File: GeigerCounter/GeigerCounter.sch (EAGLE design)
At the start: 5 parts, among them IC1 OPAMP-DUALU

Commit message: preliminary schematic work
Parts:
- added C2, C3, C4, C5, C6: (no value), SparkFun-Passives:CAPPTH2
- added H1, H2, H3, H4: MOUNT-HOLE3.0, holes:MOUNT-HOLE3.0
- added IC2: OPAMP-DUALU, SparkFun-AnalogIC:OPAMP-DUALU
- added R10, R11, R12, R13, R14, R15, R16, R18, R19, R2, R20, R22, R3, R4, R5, R6, R7, R8, R9: (no value), SparkFun-Passives:RESISTORAXIAL-0.3
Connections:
- new net N$1: C3.2, R3.1
- new net N$10: C4.2, IC2A.OUT, R12.2, R14.2, R15.1
- new net N$11: C4.1, IC2A.-IN, R12.1, R14.1
- new net N$12: C5.1, R15.2
- new net N$13: C5.2, R13.1
- new net N$14: C6.1, IC2B.-IN, R18.1, R19.1, R8.2
- new net N$15: C6.2, IC2B.OUT, R18.2, R19.2, R20.1
- new net N$2: D1.A, R9.1
- new net N$3: C2.2, IC1A.OUT, R10.2, R11.1, R2.2
- new net N$4: IC2B.+IN, R13.2, R16.2
- new net N$5: D1.C, R22.1
- new net N$6: C2.1, IC1A.-IN, R10.1, R2.1
- new net N$7: C3.1, R11.2
- new net N$8: C1.1, IC1B.-IN, R3.2, R5.1, R6.1
- new net N$9: C1.2, IC1B.OUT, R5.2, R6.2, R7.1
- new net VCC_1.25: IC1A.+IN, IC1B.+IN, R1.2, R4.1
- net GND: now also IC1A.V-, IC2A.+IN, IC2A.V-, R1.1, R16.1, R8.1
- net VCC: now also IC1A.V+, IC2A.V+, R4.2
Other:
- moved on the sheet: C1, D1, IC1A, IC1B, R1, U$1

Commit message: all components placed in schematic
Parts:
- added C10, C8: 0.1uF, SparkFun-Passives:CAPPTH2
- added C7, C9: 2.2uF, SparkFun-Passives:CAPPTH2
- added R17, R21, R23, R24: DNP, SparkFun-Passives:RESISTORAXIAL-0.3
- added R25, R26: 0, SparkFun-Passives:RESISTORAXIAL-0.3
- C1, C6, R12, R18, R2, R22, R5, R9: value (none) -> DNP
- C2, C4: value (none) -> 2pF
- C3, C5: value (none) -> 100pF
- R1, R4: value (none) -> 1k
- R10, R14: value (none) -> 10 MEGA
- R11, R13, R15, R20, R7: value (none) -> 0
- R16, R3, R8: value (none) -> 10k
- R19, R6: value (none) -> 100k
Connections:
- new net N$16: R26.1, R7.2
- new net N$17: C1.1, R24.1, R25.2
- new net N$20: C6.1, R23.1, R26.2
- new net N$21: R20.2, R25.1
- net GND: now also C1.2, C10.1, C6.2, C7.1, C8.1, C9.1, R9.2
- net N$11: now also R21.2
- net N$14: no longer C6.1
- net N$15: no longer C6.2
- net N$2: now also R17.1
- net N$5: now also R21.1
- net N$6: now also R17.2
- net N$8: no longer C1.1
- net N$9: no longer C1.2
- net P3.4: now also R24.2
- net P3.5: now also R23.2
- net VCC: now also C10.2, C7.2, C8.2, C9.2
- net VCC_1.25: now also R22.2
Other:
- moved on the sheet: C1, C6, D1, H1, H2, H3, H4, R10, R12, R14, R18, R2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

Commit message: Added header pins as well as cleaned up schematic a bit. Also added test points
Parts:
- removed R17, R21, R22, R9: DNP, SparkFun-Passives:RESISTORAXIAL-0.3
- removed R20, R26: 0, SparkFun-Passives:RESISTORAXIAL-0.3
- added TP_GND, TP_INV1, TP_INV2, TP_POS1, TP_POS2, TP_VCC: PTR1PAD1-20, testpad:PTR1PAD1-20
- added U$2: M04X2, SparkFun-Connectors:M04X2
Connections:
- removed net N$20: C6.1, R23.1, R26.2
- removed net N$21: R20.2, R25.1
- net GND: now also TP_GND.TP, U$2.4; no longer R9.2
- net N$11: now also U$2.8; no longer R21.2
- net N$12: now also TP_POS1.TP
- net N$15: now also R25.1, TP_POS2.TP; no longer R20.1
- net N$16: now also C6.1, R23.1; no longer R26.1
- net N$2: now also D1.C, U$2.5, U$2.7; no longer D1.A, R17.1, R9.1
- net N$5: now also D1.A, U$2.1, U$2.3; no longer D1.C, R21.1, R22.1
- net N$6: now also U$2.2; no longer R17.2
- net N$7: now also TP_INV1.TP
- net N$9: now also TP_INV2.TP
- net VCC: now also TP_VCC.TP
- net VCC_1.25: now also U$2.6; no longer R22.2
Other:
- note added: "Access ID: 4841"
- note added: "Decoupling Caps for IC1"
- note added: "Decoupling Caps for IC2"
- note added: "Web ID: 49211282"
- moved on the sheet: D1, R25, R7

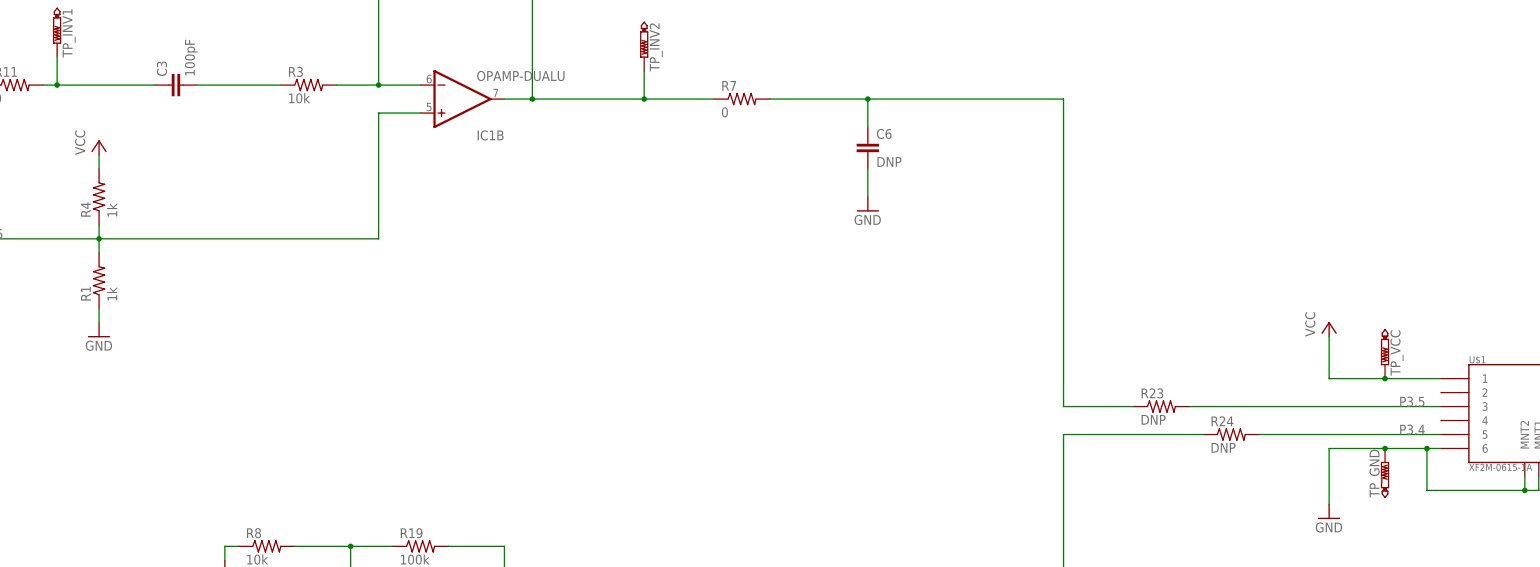
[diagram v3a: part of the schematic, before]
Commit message: Updated with new connector on output
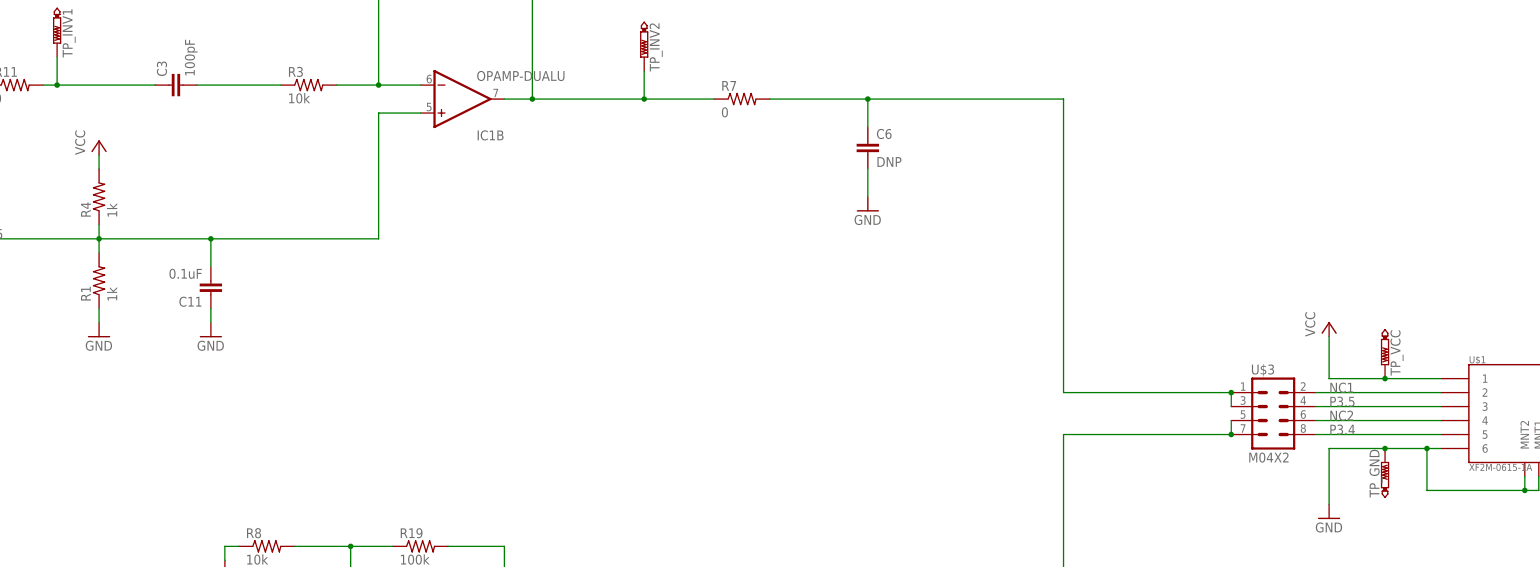
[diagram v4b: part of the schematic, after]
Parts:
- removed R23, R24: DNP, SparkFun-Passives:RESISTORAXIAL-0.3
- added C11: 0.1uF, SparkFun-Passives:CAPPTH2
- added U$3: M04X2, SparkFun-Connectors:M04X2
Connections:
- new net NC1: U$1.2, U$3.2
- new net NC2: U$1.4, U$3.6
- net GND: now also C11.1
- net N$16: now also U$3.1, U$3.3; no longer R23.1
- net N$17: now also U$3.5, U$3.7; no longer R24.1
- net P3.4: now also U$3.8; no longer R24.2
- net P3.5: now also U$3.4; no longer R23.2
- net VCC_1.25: now also C11.2
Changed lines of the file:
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@@
 <part name="P+8" library="supply1" deviceset="VCC" device=""/>
 <part name="GND12" library="supply1" deviceset="GND" device=""/>
-<part name="R23" library="SparkFun-Passives" deviceset="RESISTOR" device="AXIAL-0.3" value="DNP"/>
-<part name="R24" library="SparkFun-Passives" deviceset="RESISTOR" device="AXIAL-0.3" value="DNP"/>
 <part name="R25" library="SparkFun-Passives" deviceset="RESISTOR" device="AXIAL-0.3" value="0"/>
 <part name="C1" library="SparkFun-Passives" deviceset="CAP" device="PTH2" value="DNP"/>
@@
 <part name="TP_POS2" library="testpad" deviceset="PTR1" device="PAD1-20"/>
 <part name="U$2" library="SparkFun-Connectors" deviceset="M04X2" device=""/>
+<part name="C11" library="SparkFun-Passives" deviceset="CAP" device="PTH2" value="0.1uF"/>
+<part name="GND15" library="supply1" deviceset="GND" device=""/>
+<part name="U$3" library="SparkFun-Connectors" deviceset="M04X2" device=""/>
 </parts>
 <sheets>
@@
 <instance part="P+8" gate="VCC" x="73.66" y="71.12"/>
 <instance part="GND12" gate="1" x="35.56" y="96.52"/>
-<instance part="R23" gate="G$1" x="360.68" y="99.06"/>
-<instance part="R24" gate="G$1" x="373.38" y="93.98"/>
 <instance part="R25" gate="G$1" x="284.48" y="38.1"/>
 <instance part="C1" gate="G$1" x="304.8" y="27.94"/>
@@
 <instance part="TP_POS2" gate="G$1" x="264.16" y="45.72" rot="R180"/>
 <instance part="U$2" gate="G$1" x="25.4" y="104.14"/>
+<instance part="C11" gate="G$1" x="187.96" y="121.92" rot="R180"/>
+<instance part="GND15" gate="1" x="187.96" y="111.76"/>
+<instance part="U$3" gate="G$1" x="381" y="96.52"/>
 </instances>
 <busses>
@@
 <pinref part="GND12" gate="1" pin="GND"/>
 </segment>
+<segment>
+<pinref part="C11" gate="G$1" pin="1"/>
+<wire x1="187.96" y1="116.84" x2="187.96" y2="114.3" width="0.1524" layer="91"/>
+<pinref part="GND15" gate="1" pin="GND"/>
+</segment>
 </net>
 <net name="P3.5" class="0">
 <segment>
-<label x="403.86" y="99.06" size="1.778" layer="95"/>
+<label x="391.16" y="99.06" size="1.778" layer="95"/>
 <pinref part="U$1" gate="P$1" pin="3"/>
-<pinref part="R23" gate="G$1" pin="2"/>
-<wire x1="365.76" y1="99.06" x2="411.48" y2="99.06" width="0.1524" layer="91"/>
+<wire x1="388.62" y1="99.06" x2="411.48" y2="99.06" width="0.1524" layer="91"/>
+<pinref part="U$3" gate="G$1" pin="4"/>
 </segment>
 </net>
 <net name="P3.4" class="0">
 <segment>
-<label x="403.86" y="93.98" size="1.778" layer="95"/>
+<label x="391.16" y="93.98" size="1.778" layer="95"/>
 <pinref part="U$1" gate="P$1" pin="5"/>
-<pinref part="R24" gate="G$1" pin="2"/>
-<wire x1="378.46" y1="93.98" x2="411.48" y2="93.98" width="0.1524" layer="91"/>
+<wire x1="388.62" y1="93.98" x2="411.48" y2="93.98" width="0.1524" layer="91"/>
+<pinref part="U$3" gate="G$1" pin="8"/>
 </segment>
 </net>
@@
 <wire x1="226.06" y1="152.4" x2="218.44" y2="152.4" width="0.1524" layer="91"/>
 <wire x1="218.44" y1="152.4" x2="218.44" y2="129.54" width="0.1524" layer="91"/>
-<wire x1="218.44" y1="129.54" x2="167.64" y2="129.54" width="0.1524" layer="91"/>
+<wire x1="218.44" y1="129.54" x2="187.96" y2="129.54" width="0.1524" layer="91"/>
 <junction x="167.64" y="129.54"/>
+<wire x1="187.96" y1="129.54" x2="167.64" y2="129.54" width="0.1524" layer="91"/>
 <wire x1="167.64" y1="129.54" x2="104.14" y2="129.54" width="0.1524" layer="91"/>
 <wire x1="104.14" y1="129.54" x2="104.14" y2="154.94" width="0.1524" layer="91"/>
@@
 <wire x1="33.02" y1="104.14" x2="48.26" y2="104.14" width="0.1524" layer="91"/>
 <wire x1="48.26" y1="104.14" x2="48.26" y2="154.94" width="0.1524" layer="91"/>
+<pinref part="C11" gate="G$1" pin="2"/>
+<wire x1="187.96" y1="124.46" x2="187.96" y2="129.54" width="0.1524" layer="91"/>
+<junction x="187.96" y="129.54"/>
 </segment>
 </net>
@@
 <wire x1="304.8" y1="38.1" x2="304.8" y2="33.02" width="0.1524" layer="91"/>
 <wire x1="342.9" y1="38.1" x2="342.9" y2="93.98" width="0.1524" layer="91"/>
-<pinref part="R24" gate="G$1" pin="1"/>
-<wire x1="342.9" y1="93.98" x2="368.3" y2="93.98" width="0.1524" layer="91"/>
 <wire x1="304.8" y1="38.1" x2="342.9" y2="38.1" width="0.1524" layer="91"/>
 <junction x="304.8" y="38.1"/>
+<pinref part="U$3" gate="G$1" pin="7"/>
+<wire x1="373.38" y1="93.98" x2="342.9" y2="93.98" width="0.1524" layer="91"/>
+<pinref part="U$3" gate="G$1" pin="5"/>
+<wire x1="373.38" y1="96.52" x2="373.38" y2="93.98" width="0.1524" layer="91"/>
+<junction x="373.38" y="93.98"/>
 </segment>
 </net>
@@
 <wire x1="307.34" y1="154.94" x2="307.34" y2="149.86" width="0.1524" layer="91"/>
 <wire x1="307.34" y1="154.94" x2="342.9" y2="154.94" width="0.1524" layer="91"/>
-<wire x1="342.9" y1="154.94" x2="342.9" y2="99.06" width="0.1524" layer="91"/>
+<wire x1="342.9" y1="154.94" x2="342.9" y2="101.6" width="0.1524" layer="91"/>
 <junction x="307.34" y="154.94"/>
-<pinref part="R23" gate="G$1" pin="1"/>
-<wire x1="342.9" y1="99.06" x2="355.6" y2="99.06" width="0.1524" layer="91"/>
+<pinref part="U$3" gate="G$1" pin="1"/>
+<wire x1="373.38" y1="101.6" x2="342.9" y2="101.6" width="0.1524" layer="91"/>
+<pinref part="U$3" gate="G$1" pin="3"/>
+<wire x1="373.38" y1="99.06" x2="373.38" y2="101.6" width="0.1524" layer="91"/>
+<junction x="373.38" y="101.6"/>
 </segment>
 </net>
@@
 </segment>
 </net>
+<net name="NC1" class="0">
+<segment>
+<pinref part="U$1" gate="P$1" pin="2"/>
+<wire x1="411.48" y1="101.6" x2="388.62" y2="101.6" width="0.1524" layer="91"/>
+<label x="391.16" y="101.6" size="1.778" layer="95"/>
+<pinref part="U$3" gate="G$1" pin="2"/>
+</segment>
+</net>
+<net name="NC2" class="0">
+<segment>
+<pinref part="U$1" gate="P$1" pin="4"/>
+<wire x1="411.48" y1="96.52" x2="388.62" y2="96.52" width="0.1524" layer="91"/>
+<label x="391.16" y="96.52" size="1.778" layer="95"/>
+<pinref part="U$3" gate="G$1" pin="6"/>
+</segment>
+</net>

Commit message: Revised schematic based on working breadboard. Changed footprints to SMD pads.
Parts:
- removed C10, C11, C8: 0.1uF, SparkFun-Passives:CAPPTH2
- removed C9: 2.2uF, SparkFun-Passives:CAPPTH2
- removed IC2: OPAMP-DUALU, SparkFun-AnalogIC:OPAMP-DUALU
- removed R16: 10k, SparkFun-Passives:RESISTORAXIAL-0.3
- removed R18: DNP, SparkFun-Passives:RESISTORAXIAL-0.3
- removed R19: 100k, SparkFun-Passives:RESISTORAXIAL-0.3
- removed R25: 0, SparkFun-Passives:RESISTORAXIAL-0.3
- removed TP_INV1, TP_INV2, TP_POS1, TP_POS2: PTR1PAD1-20, testpad:PTR1PAD1-20
- removed U$2, U$3: M04X2, SparkFun-Connectors:M04X2
- added D2: DNP, SparkFun-DiscreteSemi:DIODESOT23
- added R9: 0, SparkFun-Passives:RESISTOR0603-RES
- added TP_AMP, TP_ENV, TP_GND1, TP_GND2, TP_PRE_AMP, TP_RC, TP_VBIAS, TP_VCC1: PTR1PAD1-20, testpad:PTR1PAD1-20
- C1: value DNP -> 15pF; device SparkFun-Passives:CAPPTH2 -> SparkFun-Passives:CAP0603-CAP
- C2: value 2pF -> 100p; device SparkFun-Passives:CAPPTH2 -> SparkFun-Passives:CAP0603-CAP
- C3: value 100pF -> 0.1u; device SparkFun-Passives:CAPPTH2 -> SparkFun-Passives:CAP0603-CAP
- C4: value 2pF -> DNP; device SparkFun-Passives:CAPPTH2 -> SparkFun-Passives:CAP0603-CAP
- C5: value 100pF -> DNP; device SparkFun-Passives:CAPPTH2 -> SparkFun-Passives:CAP0603-CAP
- C6: value DNP -> 2.2uF; device SparkFun-Passives:CAPPTH2 -> SparkFun-Passives:CAP0603-CAP
- C7: value 2.2uF -> 0.1uF; device SparkFun-Passives:CAPPTH2 -> SparkFun-Passives:CAP0603-CAP
- R1: value 1k -> 10M; device SparkFun-Passives:RESISTORAXIAL-0.3 -> SparkFun-Passives:RESISTOR0603-RES
- R10, R14: value 10 MEGA -> 0; device SparkFun-Passives:RESISTORAXIAL-0.3 -> SparkFun-Passives:RESISTOR0603-RES
- R11, R13, R15, R2, R6, R8: device SparkFun-Passives:RESISTORAXIAL-0.3 -> SparkFun-Passives:RESISTOR0603-RES
- R12: value DNP -> 0; device SparkFun-Passives:RESISTORAXIAL-0.3 -> SparkFun-Passives:RESISTOR0603-RES
- R3: value 10k -> 0; device SparkFun-Passives:RESISTORAXIAL-0.3 -> SparkFun-Passives:RESISTOR0603-RES
- R4: value 1k -> 100; device SparkFun-Passives:RESISTORAXIAL-0.3 -> SparkFun-Passives:RESISTOR0603-RES
- R5: value DNP -> 100; device SparkFun-Passives:RESISTORAXIAL-0.3 -> SparkFun-Passives:RESISTOR0603-RES
- R7: value 0 -> DNP; device SparkFun-Passives:RESISTORAXIAL-0.3 -> SparkFun-Passives:RESISTOR0603-RES
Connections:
- removed net N$1: C3.2, R3.1
- removed net N$10: C4.2, IC2A.OUT, R12.2, R14.2, R15.1
- removed net N$11: C4.1, IC2A.-IN, R12.1, R14.1, U$2.8
- removed net N$12: C5.1, R15.2, TP_POS1.TP
- removed net N$13: C5.2, R13.1
- removed net N$14: IC2B.-IN, R18.1, R19.1, R8.2
- removed net N$15: IC2B.OUT, R18.2, R19.2, R25.1, TP_POS2.TP
- removed net N$16: C6.1, R7.2, U$3.1, U$3.3
- removed net N$17: C1.1, R25.2, U$3.5, U$3.7
- removed net N$2: D1.C, U$2.5, U$2.7
- removed net N$3: C2.2, IC1A.OUT, R10.2, R11.1, R2.2
- removed net N$4: IC2B.+IN, R13.2, R16.2
- removed net N$5: D1.A, U$2.1, U$2.3
- removed net N$6: C2.1, IC1A.-IN, R10.1, R2.1, U$2.2
- removed net N$7: C3.1, R11.2, TP_INV1.TP
- removed net N$8: IC1B.-IN, R3.2, R5.1, R6.1
- removed net N$9: IC1B.OUT, R5.2, R6.2, R7.1, TP_INV2.TP
- new net ENV_DETEC_OUT: C4.1, D2.C, R11.2, R9.1, TP_ENV.TP
- new net IC1A_N: C1.1, D1.A, IC1A.-IN, R1.2, R2.2
- new net IC1A_OUT: C1.2, IC1A.OUT, R1.1, R2.1, R3.2
- new net IC1B_N: IC1B.-IN, R6.1, R7.1, R8.2
- new net IC1B_OUT: D2.A, IC1B.OUT, R11.1, R6.2, R7.2, TP_AMP.TP
- new net INV_AMP_INPUT: C2.2, R8.1
- new net OUTPUT: R10.2, R12.1, R13.1, R14.1, R15.1
- new net PRE_AMP: C2.1, R3.1, TP_PRE_AMP.TP
- new net RC_OUT: C5.1, R10.1, R9.2, TP_RC.TP
- net GND: now also C3.1, C4.2, C5.2, C7.2, R4.2, TP_GND1.TP, TP_GND2.TP; no longer C1.2, C10.1, C11.1, C7.1, C8.1, C9.1, IC2A.+IN, IC2A.V-, R1.1, R16.1, R8.1, U$2.4
- net NC1: now also R13.2; no longer U$3.2
- net NC2: now also R14.2; no longer U$3.6
- net P3.4: now also R15.2; no longer U$3.8
- net P3.5: now also R12.2; no longer U$3.4
- net VCC: now also C6.1, C7.1, R5.1, TP_VCC1.TP; no longer C10.2, C7.2, C8.2, C9.2, IC2A.V+, R4.2
- net VCC_1.25: now also C3.2, D1.C, R5.2, TP_VBIAS.TP; no longer C11.2, R1.2, U$2.6
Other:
- note added: "Decoupling Cap for VBIAS"
- note removed: "Access ID: 4841"
- note removed: "Decoupling Caps for IC2"
- note removed: "Web ID: 49211282"
- moved on the sheet: C1, C2, C3, C4, C5, C6, C7, D1, H1, H2, H3, H4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

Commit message: Layout completed. Routed not yet started.
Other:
- note added: "1"
- note added: "Geiger Counter Daughter Board"
- moved on the sheet: C1, C2, C3, C4, C5, C6, C7, D1, D2, H1, H2, H3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

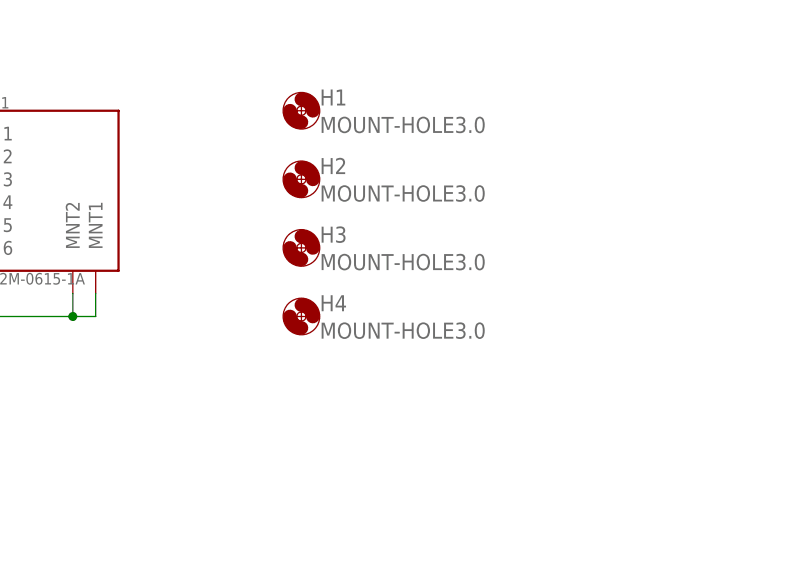
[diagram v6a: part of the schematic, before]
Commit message: Basic routing completed. No pours yet.
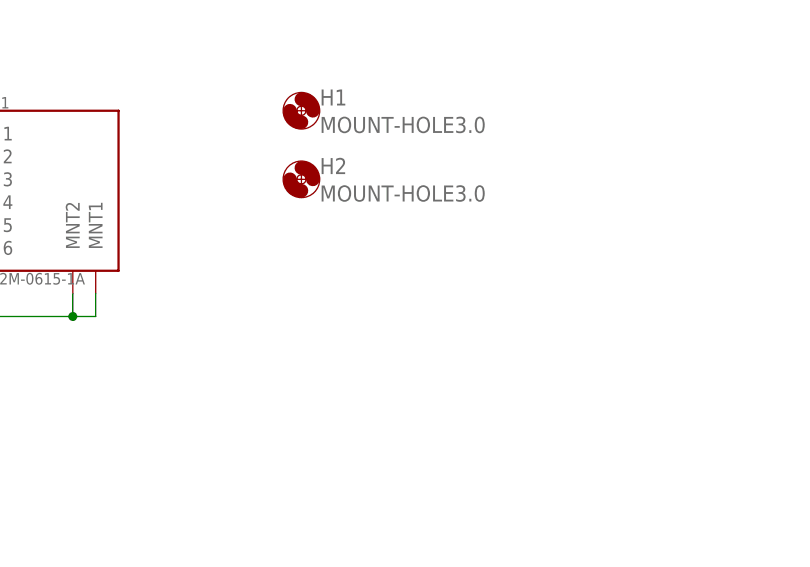
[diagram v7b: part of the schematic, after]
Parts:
- removed H3, H4: MOUNT-HOLE3.0, holes:MOUNT-HOLE3.0
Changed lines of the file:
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@@
 <part name="H1" library="holes" deviceset="MOUNT-HOLE" device="3.0"/>
 <part name="H2" library="holes" deviceset="MOUNT-HOLE" device="3.0"/>
-<part name="H3" library="holes" deviceset="MOUNT-HOLE" device="3.0"/>
-<part name="H4" library="holes" deviceset="MOUNT-HOLE" device="3.0"/>
 <part name="GND8" library="supply1" deviceset="GND" device=""/>
 <part name="GND9" library="supply1" deviceset="GND" device=""/>
@@
 <instance part="H1" gate="G$1" x="482.6" y="238.76"/>
 <instance part="H2" gate="G$1" x="482.6" y="231.14"/>
-<instance part="H3" gate="G$1" x="482.6" y="223.52"/>
-<instance part="H4" gate="G$1" x="482.6" y="215.9"/>
 <instance part="GND8" gate="1" x="86.36" y="254"/>
 <instance part="GND9" gate="1" x="99.06" y="254"/>

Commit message: More routing
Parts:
- removed TP_GND2: PTR1PAD1-20, testpad:PTR1PAD1-20
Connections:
- net GND: no longer TP_GND2.TP
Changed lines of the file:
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@@
 <part name="TP_VCC1" library="testpad" deviceset="PTR1" device="PAD1-20"/>
 <part name="TP_GND1" library="testpad" deviceset="PTR1" device="PAD1-20"/>
-<part name="TP_GND2" library="testpad" deviceset="PTR1" device="PAD1-20"/>
 <part name="TP_VBIAS" library="testpad" deviceset="PTR1" device="PAD1-20"/>
 <part name="D2" library="SparkFun-DiscreteSemi" deviceset="DIODE" device="SOT23" value="DNP"/>
@@
 <instance part="TP_VCC1" gate="G$1" x="426.72" y="238.76" rot="R180"/>
 <instance part="TP_GND1" gate="G$1" x="436.88" y="220.98"/>
-<instance part="TP_GND2" gate="G$1" x="426.72" y="220.98"/>
 <instance part="TP_VBIAS" gate="G$1" x="144.78" y="210.82" rot="R180"/>
 <instance part="D2" gate="G$1" x="281.94" y="233.68"/>
@@
 <wire x1="439.42" y1="223.52" x2="436.88" y2="223.52" width="0.1524" layer="91"/>
 <wire x1="436.88" y1="223.52" x2="431.8" y2="223.52" width="0.1524" layer="91"/>
-<wire x1="431.8" y1="223.52" x2="426.72" y2="223.52" width="0.1524" layer="91"/>
-<wire x1="426.72" y1="223.52" x2="421.64" y2="223.52" width="0.1524" layer="91"/>
+<wire x1="431.8" y1="223.52" x2="421.64" y2="223.52" width="0.1524" layer="91"/>
 <wire x1="421.64" y1="223.52" x2="421.64" y2="213.36" width="0.1524" layer="91"/>
 <pinref part="U$1" gate="P$1" pin="6"/>
@@
 <pinref part="TP_GND1" gate="G$1" pin="TP"/>
 <junction x="436.88" y="223.52"/>
-<pinref part="TP_GND2" gate="G$1" pin="TP"/>
-<junction x="426.72" y="223.52"/>
 </segment>
 <segment>
